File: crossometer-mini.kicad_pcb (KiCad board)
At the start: 2 copper layers, 38 x 60 mm, 63 parts, among them J1 UART, J2 BAT, J3 AUX, J4 I²C, J5 USB_C_Receptacle_USB2.0, J6 Micro_SD_Card_Det, Q1 2N7002, Q2 CJ2301, Q3 UMH3N, SW1 IO0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

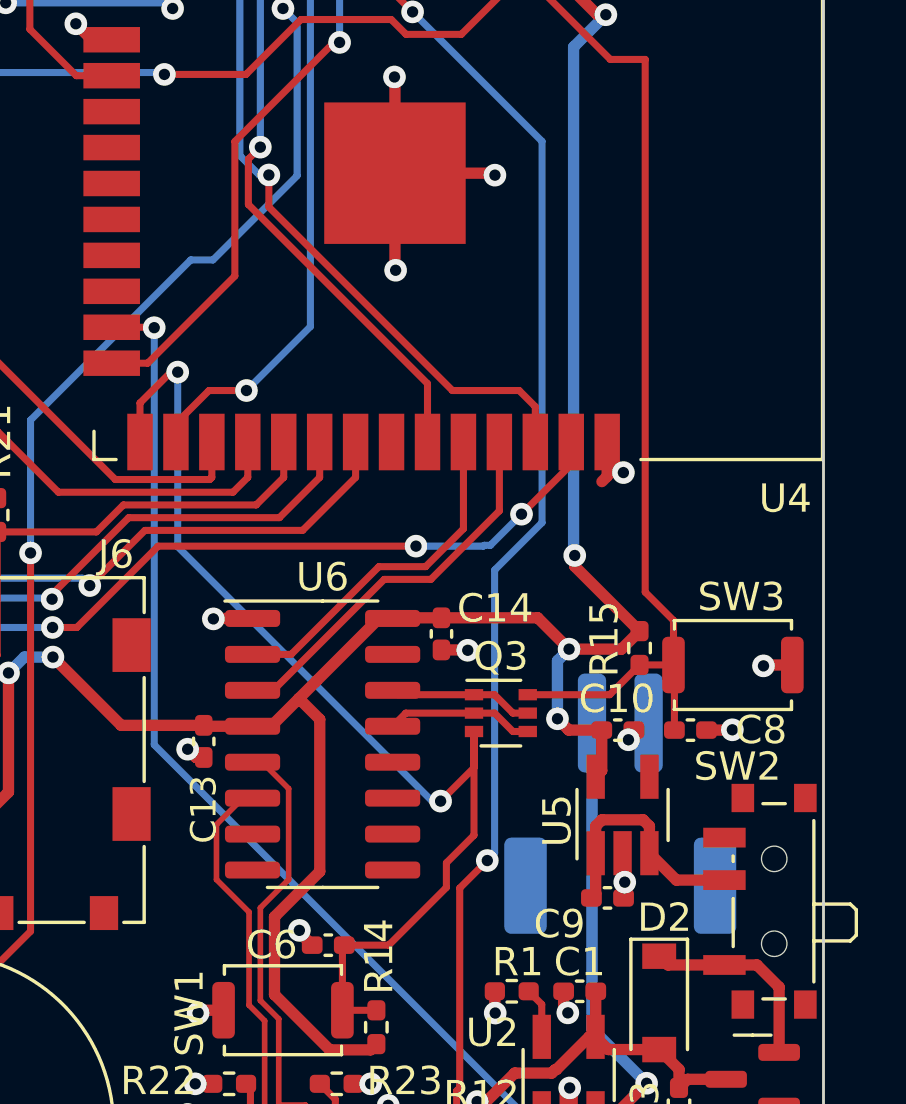
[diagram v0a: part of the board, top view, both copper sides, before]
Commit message: add LCSC field to schematic
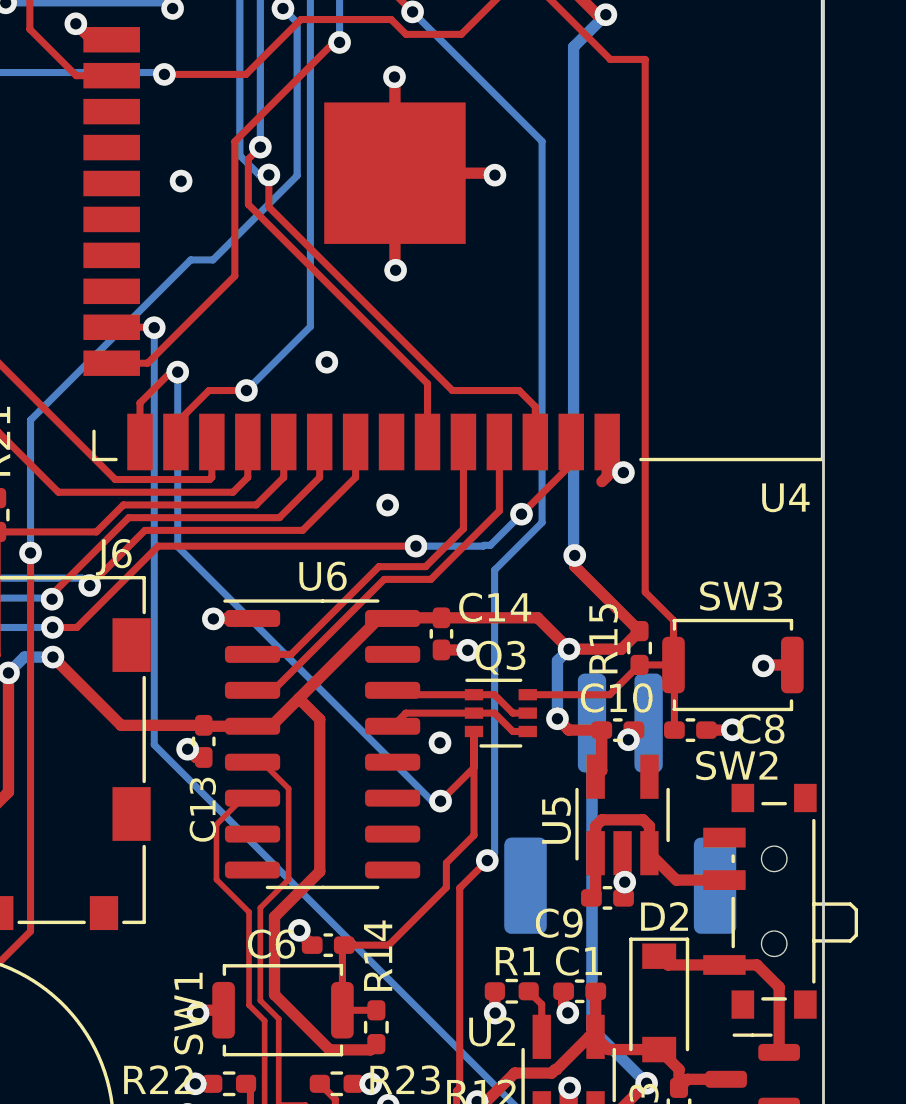
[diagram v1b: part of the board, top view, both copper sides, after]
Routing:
- net GND: vias 42 -> 46
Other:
- board text added: "github.com/fredszaq/crossometer-mini"
